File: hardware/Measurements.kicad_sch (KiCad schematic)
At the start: 10 parts, among them IC1 MCP1501-10E_SN, IC7 MCP3562T-E_NC, IC8 REF196GSZ-REEL

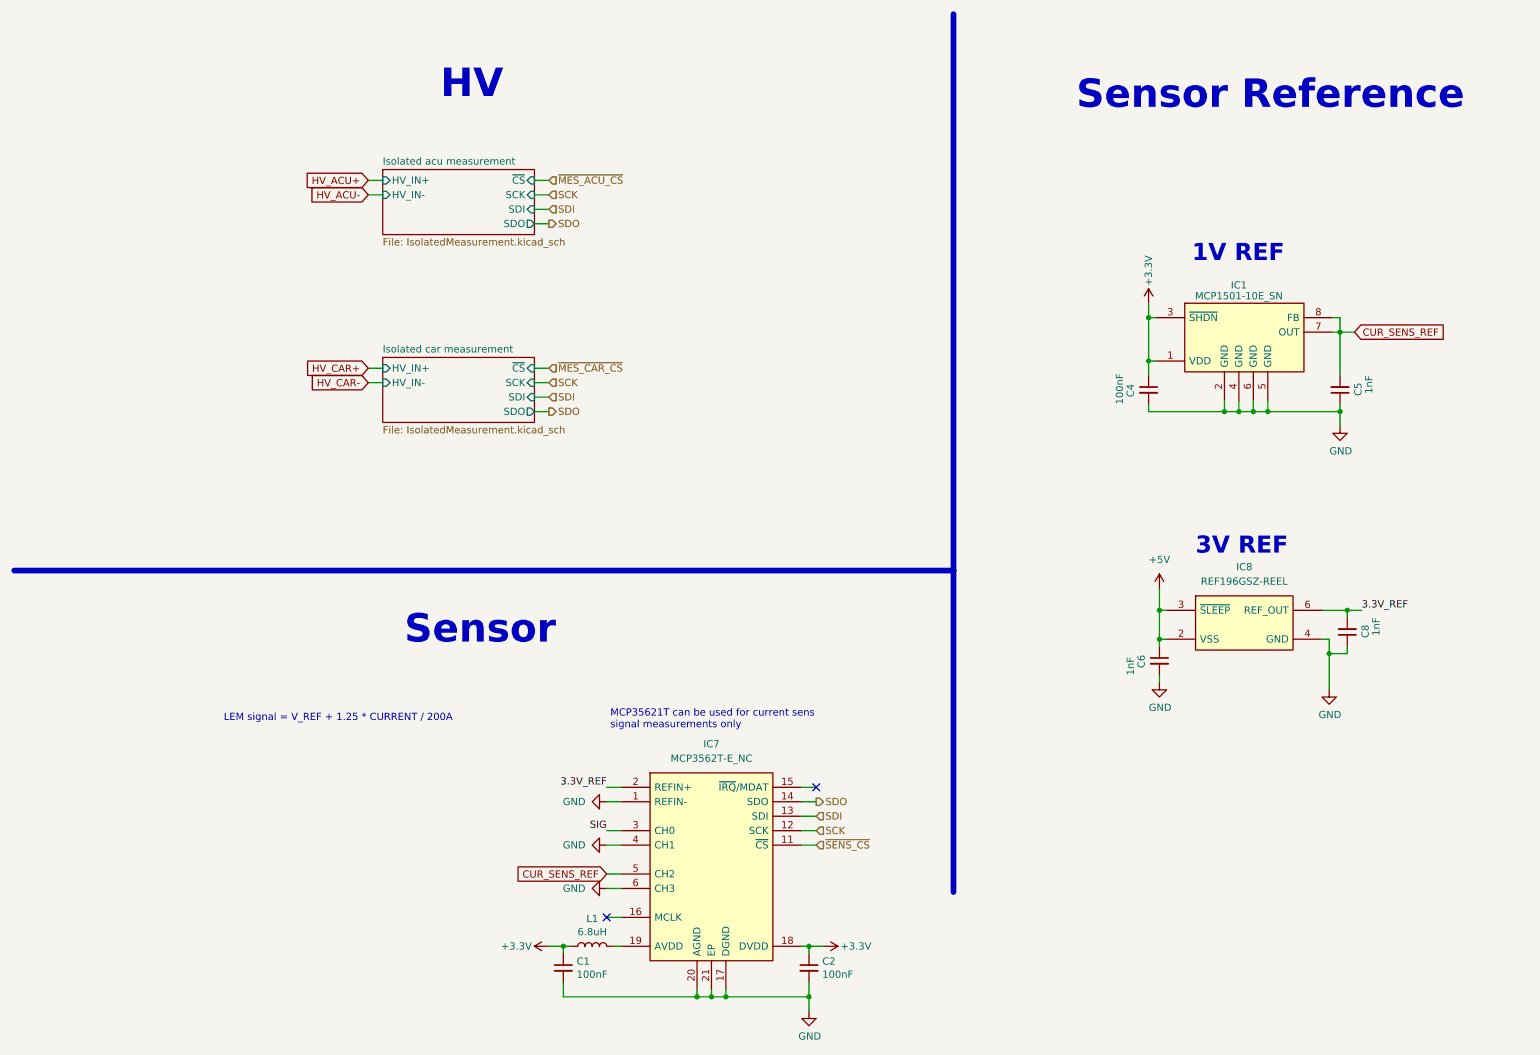
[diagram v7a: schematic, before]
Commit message: measurments section changes, sorted components on the board into groups, changed main connector and added seprate for AIRs, added IMD PWM input as well as AIR fault detection
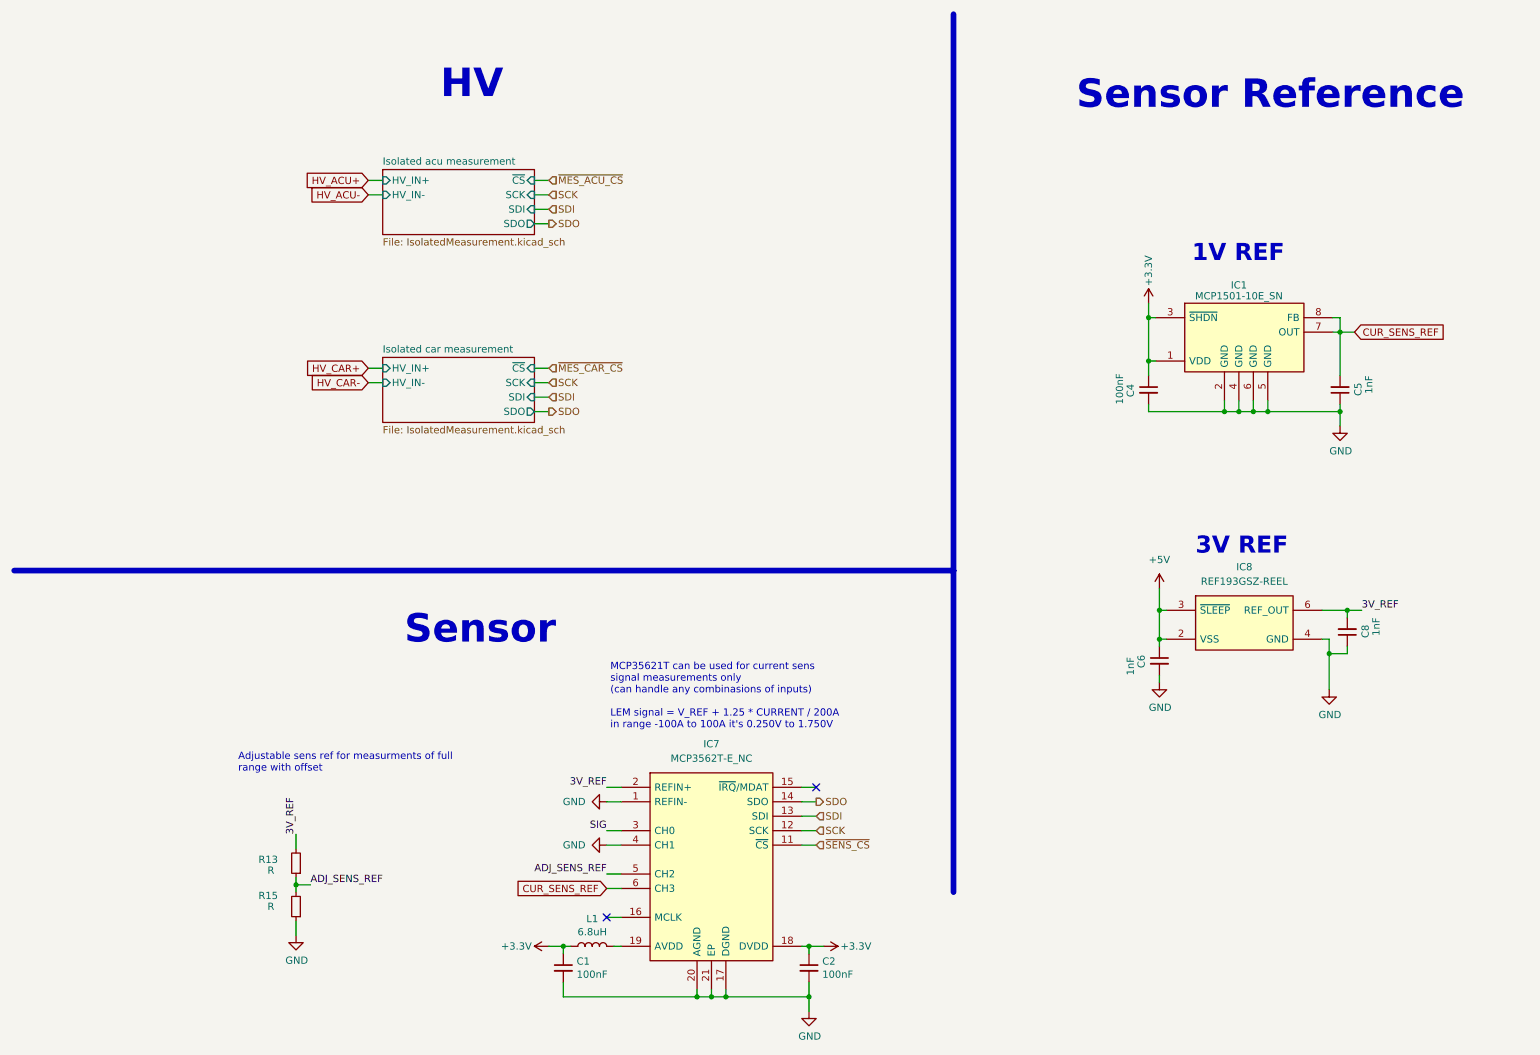
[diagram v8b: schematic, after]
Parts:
- added R13, R15: R, Resistor_SMD:R_0603_1608Metric, symbol Device:R_Small
- IC8: value REF196GSZ-REEL -> REF193GSZ-REEL
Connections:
- net CUR_SENS_REF: now also IC7.6 (CH3); no longer IC7.5 (CH2)
- net GND: now also R15.1; no longer IC7.6 (CH3)
- net 3.3V_REF renamed 3V_REF
- net 3V_REF: now also R13.2
- new net ADJ_SENS_REF: IC7.5 (CH2), R13.1, R15.2
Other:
- note added: "Adjustable sens ref for measurments of full range with offset"
- note added: "MCP35621T can be used for current sens signal measurements only (can handle any combinasions of inputs) LEM signal = V_REF + 1.25 * CURRENT / 200A in range -100A to 100A it's 0.250V to 1.750V"
- note removed: "LEM signal = V_REF + 1.25 * CURRENT / 200A"
- note removed: "MCP35621T can be used for current sens signal measurements only"
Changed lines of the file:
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@@
   (junction (at 211.455 73.025) (diameter 0) (color 0 0 0 0)
+  )
+  (junction (at 61.595 165.1) (diameter 0) (color 0 0 0 0)
   )
   (junction (at 227.33 81.915) (diameter 0) (color 0 0 0 0)
@@
     (stroke (width 0) (type default) (color 0 0 0 0))
   )
+  (wire (pts (xy 61.595 163.83) (xy 61.595 165.1))
+    (stroke (width 0) (type default) (color 0 0 0 0))
+  )
   (wire (pts (xy 74.295 74.295) (xy 76.835 74.295))
     (stroke (width 0) (type default) (color 0 0 0 0))
@@
   )
   (wire (pts (xy 224.79 81.915) (xy 227.33 81.915))
+    (stroke (width 0) (type default) (color 0 0 0 0))
+  )
+  (wire (pts (xy 61.595 165.1) (xy 64.135 165.1))
     (stroke (width 0) (type default) (color 0 0 0 0))
   )
@@
     (stroke (width 1) (type default) (color 132 0 0 1))
   )
+  (wire (pts (xy 61.595 165.1) (xy 61.595 166.37))
+    (stroke (width 0) (type default) (color 0 0 0 0))
+  )
   (wire (pts (xy 151.765 184.785) (xy 151.765 187.325))
     (stroke (width 0) (type default) (color 0 0 0 0))
@@
     (stroke (width 0) (type default) (color 0 0 0 0))
   )
+  (wire (pts (xy 61.595 171.45) (xy 61.595 173.99))
+    (stroke (width 0) (type default) (color 0 0 0 0))
+  )
   (wire (pts (xy 224.79 80.01) (xy 224.79 81.915))
     (stroke (width 0) (type default) (color 0 0 0 0))
@@
   )
   (wire (pts (xy 151.765 175.895) (xy 154.305 175.895))
+    (stroke (width 0) (type default) (color 0 0 0 0))
+  )
+  (wire (pts (xy 61.595 156.21) (xy 61.595 158.75))
     (stroke (width 0) (type default) (color 0 0 0 0))
   )
@@
     (effects (font (size 5 5) (thickness 1) bold) (justify left bottom))
   )
+  (text "Adjustable sens ref for measurments of full\nrange with offset"
+    (at 51.435 145.415 0)
+    (effects (font (size 1.27 1.27)) (justify left bottom))
+  )
   (text "Sensor Reference" (at 198.755 29.21 0)
     (effects (font (size 5 5) (thickness 1) bold) (justify left bottom))
   )
-  (text "MCP35621T can be used for current sens\nsignal measurements only"
+  (text "MCP35621T can be used for current sens\nsignal measurements only\n(can handle any combinasions of inputs)\n\nLEM signal = V_REF + 1.25 * CURRENT / 200A\nin range -100A to 100A it's 0.250V to 1.750V"
     (at 116.84 137.795 0)
     (effects (font (size 1.27 1.27)) (justify left bottom))
   )
-  (text "LEM signal = V_REF + 1.25 * CURRENT / 200A" (at 48.895 136.525 0)
-    (effects (font (size 1.27 1.27)) (justify left bottom))
-  )
   (text "Sensor" (at 80.645 123.19 0)
     (effects (font (size 5 5) (thickness 1) bold) (justify left bottom))
@@
     (effects (font (size 3 3) (thickness 1) bold) (justify left bottom))
   )
-  (label "3.3V_REF" (at 248.92 116.84 0)
+  (label "3V_REF" (at 61.595 156.21 90)
     (effects (font (size 1.27 1.27)) (justify left bottom))
+  )
+  (label "3V_REF" (at 248.92 116.84 0)
+    (effects (font (size 1.27 1.27)) (justify left bottom))
+  )
+  (label "ADJ_SENS_REF" (at 64.135 165.1 0)
+    (effects (font (size 1.27 1.27)) (justify left bottom))
+  )
+  (label "ADJ_SENS_REF" (at 116.205 163.195 180)
+    (effects (font (size 1.27 1.27)) (justify right bottom))
   )
   (label "SIG" (at 116.205 155.575 180)
     (effects (font (size 1.27 1.27)) (justify right bottom))
   )
-  (label "3.3V_REF" (at 116.205 147.955 180)
+  (label "3V_REF" (at 116.205 147.955 180)
     (effects (font (size 1.27 1.27)) (justify right bottom))
   )
@@
     )
   )
-  (global_label "CUR_SENS_REF" (shape input) (at 116.205 163.195 180) (fields_autoplaced)
+  (global_label "CUR_SENS_REF" (shape input) (at 116.205 165.735 180) (fields_autoplaced)
     (effects (font (size 1.27 1.27)) (justify right))
-    (property "Intersheet References" "${INTERSHEET_REFS}" (id 0) (at 99.6689 163.2744 0)
+    (property "Intersheet References" "${INTERSHEET_REFS}" (id 0) (at 99.6689 165.8144 0)
       (effects (font (size 1.27 1.27)) (justify right) hide)
     )
@@
   (hierarchical_label "~{SENS_CS}" (shape input) (at 153.035 158.115 0)
     (effects (font (size 1.27 1.27)) (justify left))
+  )
+  (symbol (lib_id "Device:R_Small") (at 61.595 168.91 180) (unit 1)
+    (in_bom yes) (on_board yes)
+    (property "Reference" "R15" (id 0) (at 58.42 167.005 0)
+      (effects (font (size 1.27 1.27)) (justify left))
+    )
+    (property "Value" "R" (id 1) (at 57.785 168.91 0)
+      (effects (font (size 1.27 1.27)) (justify left))
+    )
+    (property "Footprint" "Resistor_SMD:R_0603_1608Metric" (id 2) (at 61.595 168.91 0)
+      (effects (font (size 1.27 1.27)) hide)
+    )
+    (property "Datasheet" "~" (id 3) (at 61.595 168.91 0)
+      (effects (font (size 1.27 1.27)) hide)
+    )
+    (pin "1")
+    (pin "2")
   )
   (symbol (lib_id "Device:C_Small") (at 108.585 179.705 0) (unit 1)
@@
     (pin "7")
     (pin "8")
+  )
+  (symbol (lib_id "power:GND") (at 61.595 173.99 0) (unit 1)
+    (in_bom yes) (on_board yes)
+    (property "Reference" "#PWR0182" (id 0) (at 61.595 180.34 0)
+      (effects (font (size 1.27 1.27)) hide)
+    )
+    (property "Value" "GND" (id 1) (at 61.722 178.3842 0))
+    (property "Footprint" "" (id 2) (at 61.595 173.99 0)
+      (effects (font (size 1.27 1.27)) hide)
+    )
+    (property "Datasheet" "" (id 3) (at 61.595 173.99 0)
+      (effects (font (size 1.27 1.27)) hide)
+    )
+    (pin "1")
   )
   (symbol (lib_id "power:GND") (at 116.205 150.495 270) (unit 1)
@@
     (pin "6")
   )
+  (symbol (lib_id "Device:R_Small") (at 61.595 161.29 180) (unit 1)
+    (in_bom yes) (on_board yes)
+    (property "Reference" "R13" (id 0) (at 58.42 160.655 0)
+      (effects (font (size 1.27 1.27)) (justify left))
+    )
+    (property "Value" "R" (id 1) (at 57.785 162.56 0)
+      (effects (font (size 1.27 1.27)) (justify left))
+    )
+    (property "Footprint" "Resistor_SMD:R_0603_1608Metric" (id 2) (at 61.595 161.29 0)
+      (effects (font (size 1.27 1.27)) hide)
+    )
+    (property "Datasheet" "~" (id 3) (at 61.595 161.29 0)
+      (effects (font (size 1.27 1.27)) hide)
+    )
+    (pin "1")
+    (pin "2")
+  )
   (symbol (lib_id "power:GND") (at 243.205 130.81 0) (unit 1)
     (in_bom yes) (on_board yes)
@@
   (symbol (lib_id "power:+5V") (at 213.36 113.03 0) (unit 1)
     (in_bom yes) (on_board yes) (fields_autoplaced)
-    (property "Reference" "#PWR?" (id 0) (at 213.36 116.84 0)
+    (property "Reference" "#PWR0179" (id 0) (at 213.36 116.84 0)
       (effects (font (size 1.27 1.27)) hide)
     )
@@
     (pin "1")
   )
-  (symbol (lib_id "power:GND") (at 116.205 165.735 270) (unit 1)
-    (in_bom yes) (on_board yes)
-    (property "Reference" "#PWR0179" (id 0) (at 109.855 165.735 0)
-      (effects (font (size 1.27 1.27)) hide)
-    )
-    (property "Value" "GND" (id 1) (at 110.49 165.735 90))
-    (property "Footprint" "" (id 2) (at 116.205 165.735 0)
-      (effects (font (size 1.27 1.27)) hide)
-    )
-    (property "Datasheet" "" (id 3) (at 116.205 165.735 0)
-      (effects (font (size 1.27 1.27)) hide)
-    )
-    (pin "1")
-  )
   (symbol (lib_id "REF196GSZ-REEL:REF196GSZ-REEL") (at 228.6 118.745 0) (unit 1)
     (in_bom yes) (on_board yes) (fields_autoplaced)
     (property "Reference" "IC8" (id 0) (at 228.2825 109.22 0))
-    (property "Value" "REF196GSZ-REEL" (id 1) (at 228.2825 111.76 0))
+    (property "Value" "REF193GSZ-REEL" (id 1) (at 228.2825 111.76 0))
     (property "Footprint" "SOIC127P600X175-8N" (id 2) (at 257.81 116.205 0)
       (effects (font (size 1.27 1.27)) (justify left) hide)
